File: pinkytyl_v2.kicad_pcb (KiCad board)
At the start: 2 copper layers, 132 x 105.9 mm, 62 parts, among them J1 50-00174, J2 Conn_01x02, J3 USB_B_Mini, J5 Conn_02x05_Odd_Even, K0 KEYSW, K10 KEYSW, K11 KEYSW, K12 KEYSW, K13 KEYSW, K14 KEYSW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

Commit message: Adds name to silkscreen
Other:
- board text added: "ISP"
- board text added: "Pinkytyl V2 By Philip K. Gisslow 09/27/21"
- board text added: "Reset"
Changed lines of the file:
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@@
   (general
     (thickness 1.6)
-    (drawings 33)
+    (drawings 36)
     (tracks 605)
     (zones 0)
@@
     (descr "Through hole straight pin header, 1x02, 1.27mm pitch, single row")
     (tags "Through hole pin header THT 1x02 1.27mm single row")
-    (fp_text reference J2 (at -2.51 0.31 90) (layer F.SilkS)
+    (fp_text reference J2 (at -0.03 -2.34 90) (layer F.SilkS)
       (effects (font (size 1 1) (thickness 0.15)))
     )
@@
     (tags capacitor)
     (attr smd)
-    (fp_text reference C6 (at 2.69 1.52) (layer F.SilkS)
+    (fp_text reference C6 (at -4.79 0.41) (layer F.SilkS)
       (effects (font (size 1 1) (thickness 0.15)))
     )
@@
     )
   )
+  (gr_text ISP (at 186.4 116.18) (layer F.SilkS)
+    (effects (font (size 1 1) (thickness 0.15)))
+  )
+  (gr_text Reset (at 185.94 111.68) (layer F.SilkS)
+    (effects (font (size 1 1) (thickness 0.15)))
+  )
+  (gr_text "Pinkytyl V2 By\nPhilip K. Gisslow\n09/27/21" (at 174.81 117.05) (layer F.SilkS)
+    (effects (font (size 1 1) (thickness 0.15)))
+  )
   (gr_line (start 130.716898 92.180109) (end 125.716898 100.724303) (layer Edge.Cuts) (width 0.2))

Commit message: Inc
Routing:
- net VCC: track 238.5 -> 246.6 mm
- net r0: track 160.7 -> 157.3 mm
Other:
- board text added: "JLCJLCJLCJLC"
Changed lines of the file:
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@@
   (general
     (thickness 1.6)
-    (drawings 36)
-    (tracks 605)
+    (drawings 37)
+    (tracks 602)
     (zones 0)
     (modules 62)
@@
     )
   )
+  (gr_text JLCJLCJLCJLC (at 163.01 107.25) (layer F.SilkS)
+    (effects (font (size 0.9 0.9) (thickness 0.15)))
+  )
   (gr_text ISP (at 186.4 116.18) (layer F.SilkS)
     (effects (font (size 1 1) (thickness 0.15)))
@@
   (segment (start 155.17 106.02) (end 155.14 106.05) (width 0.25) (layer F.Cu) (net 1))
   (segment (start 155.17 104.87) (end 155.17 106.02) (width 0.25) (layer F.Cu) (net 1))
-  (via (at 156.67 113.63) (size 0.8) (drill 0.4) (layers F.Cu B.Cu) (net 1))
-  (segment (start 155.14 112.1) (end 156.67 113.63) (width 0.25) (layer B.Cu) (net 1))
-  (segment (start 155.14 106.05) (end 155.14 112.1) (width 0.25) (layer B.Cu) (net 1))
-  (segment (start 158.78 113.63) (end 158.92 113.77) (width 0.25) (layer F.Cu) (net 1))
-  (segment (start 156.67 113.63) (end 158.78 113.63) (width 0.25) (layer F.Cu) (net 1))
-  (segment (start 166.655001 112.694999) (end 166.92 112.959998) (width 0.25) (layer F.Cu) (net 1))
-  (segment (start 162.239132 111.305542) (end 163.628589 112.694999) (width 0.25) (layer F.Cu) (net 1))
-  (segment (start 163.628589 112.694999) (end 166.655001 112.694999) (width 0.25) (layer F.Cu) (net 1))
-  (segment (start 159.819186 111.305542) (end 162.239132 111.305542) (width 0.25) (layer F.Cu) (net 1))
-  (segment (start 158.429729 112.694999) (end 159.819186 111.305542) (width 0.25) (layer F.Cu) (net 1))
-  (segment (start 166.92 112.959998) (end 166.92 113.77) (width 0.25) (layer F.Cu) (net 1))
-  (segment (start 157.605001 112.694999) (end 158.429729 112.694999) (width 0.25) (layer F.Cu) (net 1))
-  (segment (start 156.67 113.63) (end 157.605001 112.694999) (width 0.25) (layer F.Cu) (net 1))
   (segment (start 169.93 101.24) (end 169.02 100.33) (width 0.25) (layer F.Cu) (net 1))
   (segment (start 170.82 101.24) (end 169.93 101.24) (width 0.25) (layer F.Cu) (net 1))
   (segment (start 169.02 102.83) (end 168.404999 103.445001) (width 0.25) (layer F.Cu) (net 1))
   (segment (start 169.02 100.33) (end 169.02 102.83) (width 0.25) (layer F.Cu) (net 1))
+  (segment (start 163.628589 112.694999) (end 162.239132 111.305542) (width 0.25) (layer F.Cu) (net 1))
+  (segment (start 166.92 112.77) (end 166.844999 112.694999) (width 0.25) (layer F.Cu) (net 1))
+  (via (at 161.46 117.05) (size 0.8) (drill 0.4) (layers F.Cu B.Cu) (net 1))
+  (segment (start 158.92 113.77) (end 158.920001 115.140001) (width 0.25) (layer F.Cu) (net 1))
+  (segment (start 159.788773 111.305542) (end 158.920001 112.174314) (width 0.25) (layer F.Cu) (net 1))
+  (segment (start 160.83 117.05) (end 161.46 117.05) (width 0.25) (layer F.Cu) (net 1))
+  (segment (start 158.920001 115.140001) (end 160.83 117.05) (width 0.25) (layer F.Cu) (net 1))
+  (segment (start 166.844999 112.694999) (end 163.628589 112.694999) (width 0.25) (layer F.Cu) (net 1))
+  (segment (start 162.239132 111.305542) (end 159.788773 111.305542) (width 0.25) (layer F.Cu) (net 1))
+  (segment (start 155.14 110.73) (end 161.46 117.05) (width 0.25) (layer B.Cu) (net 1))
+  (segment (start 166.92 113.77) (end 166.92 112.77) (width 0.25) (layer F.Cu) (net 1))
+  (segment (start 155.14 106.05) (end 155.14 110.73) (width 0.25) (layer B.Cu) (net 1))
+  (segment (start 158.920001 112.174314) (end 158.920001 115.140001) (width 0.25) (layer F.Cu) (net 1))
   (segment (start 116.54 44.4725) (end 115.34 44.4725) (width 0.25) (layer F.Cu) (net 2))
   (segment (start 157.06 103.91) (end 157.22 104.07) (width 0.25) (layer F.Cu) (net 2))
@@
   (segment (start 163.81609 96.82391) (end 163.85 96.79) (width 0.25) (layer F.Cu) (net 2))
   (segment (start 155.94 96.82391) (end 163.81609 96.82391) (width 0.25) (layer F.Cu) (net 2))
-  (segment (start 159.72 114.77) (end 159.72 113.77) (width 0.25) (layer F.Cu) (net 2))
-  (segment (start 161.18501 116.23501) (end 159.72 114.77) (width 0.25) (layer F.Cu) (net 2))
-  (segment (start 166.02499 116.23501) (end 161.18501 116.23501) (width 0.25) (layer F.Cu) (net 2))
-  (segment (start 166.35 115.91) (end 166.02499 116.23501) (width 0.25) (layer F.Cu) (net 2))
-  (segment (start 166.35 115.6) (end 166.35 115.91) (width 0.25) (layer F.Cu) (net 2))
   (segment (start 173.77 107.27) (end 172.04 107.27) (width 0.25) (layer F.Cu) (net 2))
   (segment (start 174.23 107.73) (end 173.77 107.27) (width 0.25) (layer F.Cu) (net 2))
@@
   (segment (start 162.2 97.994315) (end 163.404315 96.79) (width 0.25) (layer F.Cu) (net 2))
   (segment (start 162.2 98.56) (end 162.2 97.994315) (width 0.25) (layer F.Cu) (net 2))
+  (segment (start 166.02499 116.23501) (end 161.378012 116.23501) (width 0.25) (layer F.Cu) (net 2))
+  (segment (start 166.35 115.91) (end 166.02499 116.23501) (width 0.25) (layer F.Cu) (net 2))
+  (segment (start 166.35 115.6) (end 166.35 115.91) (width 0.25) (layer F.Cu) (net 2))
+  (segment (start 159.72 114.576998) (end 159.72 113.77) (width 0.25) (layer F.Cu) (net 2))
+  (segment (start 161.378012 116.23501) (end 159.72 114.576998) (width 0.25) (layer F.Cu) (net 2))
   (segment (start 163.85 99.66) (end 163.56 99.95) (width 0.25) (layer F.Cu) (net 3))
   (segment (start 163.85 98.49) (end 163.85 99.66) (width 0.25) (layer F.Cu) (net 3))
@@
   (segment (start 85.657358 123.3) (end 79.04 116.682642) (width 0.25) (layer F.Cu) (net 22))
   (segment (start 89.05 123.3) (end 85.657358 123.3) (width 0.25) (layer F.Cu) (net 22))
-  (segment (start 99.84 114.99) (end 99.84 108.82) (width 0.25) (layer F.Cu) (net 22))
-  (segment (start 142.2 88.86) (end 151.24 97.9) (width 0.25) (layer F.Cu) (net 22))
+  (segment (start 153.73 100.39) (end 153.73 107.238427) (width 0.25) (layer F.Cu) (net 22))
+  (segment (start 142.2 88.86) (end 153.73 100.39) (width 0.25) (layer F.Cu) (net 22))
   (segment (start 127.82 88.86) (end 142.2 88.86) (width 0.25) (layer F.Cu) (net 22))
+  (segment (start 121.47 95.21) (end 127.82 88.86) (width 0.25) (layer F.Cu) (net 22))
   (segment (start 113.45 95.21) (end 121.47 95.21) (width 0.25) (layer F.Cu) (net 22))
   (segment (start 99.84 108.82) (end 113.45 95.21) (width 0.25) (layer F.Cu) (net 22))
-  (segment (start 89.05 123.3) (end 92.472642 123.3) (width 0.25) (layer F.Cu) (net 22))
-  (segment (start 92.472642 123.3) (end 96.238001 119.534641) (width 0.25) (layer F.Cu) (net 22))
-  (segment (start 121.47 95.21) (end 127.82 88.86) (width 0.25) (layer F.Cu) (net 22))
+  (segment (start 99.84 114.99) (end 99.84 108.82) (width 0.25) (layer F.Cu) (net 22))
   (segment (start 96.238001 118.591999) (end 99.84 114.99) (width 0.25) (layer F.Cu) (net 22))
   (segment (start 96.238001 119.534641) (end 96.238001 118.591999) (width 0.25) (layer F.Cu) (net 22))
-  (segment (start 151.24 97.9) (end 151.24 107.103269) (width 0.25) (layer F.Cu) (net 22))
-  (segment (start 151.363146 107.27) (end 151.331573 107.238427) (width 0.25) (layer F.Cu) (net 22))
-  (segment (start 157.22 107.27) (end 151.363146 107.27) (width 0.25) (layer F.Cu) (net 22))
-  (segment (start 151.24 107.103269) (end 151.331573 107.238427) (width 0.25) (layer F.Cu) (net 22))
-  (segment (start 162.320272 120.093274) (end 162.666878 120.093274) (width 0.25) (layer F.Cu) (net 22))
-  (segment (start 157.319985 115.092987) (end 162.320272 120.093274) (width 0.25) (layer F.Cu) (net 22))
-  (segment (start 157.022987 115.092987) (end 157.319985 115.092987) (width 0.25) (layer F.Cu) (net 22))
-  (segment (start 155.876163 113.946163) (end 157.022987 115.092987) (width 0.25) (layer F.Cu) (net 22))
-  (segment (start 162.666878 120.093274) (end 163.303274 120.093274) (width 0.25) (layer F.Cu) (net 22))
-  (segment (start 151.331573 107.238427) (end 155.876163 113.946163) (width 0.25) (layer F.Cu) (net 22))
+  (segment (start 92.472642 123.3) (end 96.238001 119.534641) (width 0.25) (layer F.Cu) (net 22))
+  (segment (start 89.05 123.3) (end 92.472642 123.3) (width 0.25) (layer F.Cu) (net 22))
+  (segment (start 157.188427 107.238427) (end 157.22 107.27) (width 0.25) (layer F.Cu) (net 22))
+  (segment (start 155.758427 112.614837) (end 163.236864 120.093274) (width 0.25) (layer F.Cu) (net 22))
+  (segment (start 163.236864 120.093274) (end 163.303274 120.093274) (width 0.25) (layer F.Cu) (net 22))
+  (segment (start 155.758427 107.238427) (end 155.758427 112.614837) (width 0.25) (layer F.Cu) (net 22))
+  (segment (start 153.73 107.238427) (end 155.758427 107.238427) (width 0.25) (layer F.Cu) (net 22))
+  (segment (start 155.758427 107.238427) (end 157.188427 107.238427) (width 0.25) (layer F.Cu) (net 22))
   (segment (start 77.02 117.57) (end 77.02 116.3) (width 0.25) (layer F.Cu) (net 23))
   (segment (start 75.75 118.84) (end 77.02 117.57) (width 0.25) (layer F.Cu) (net 23))

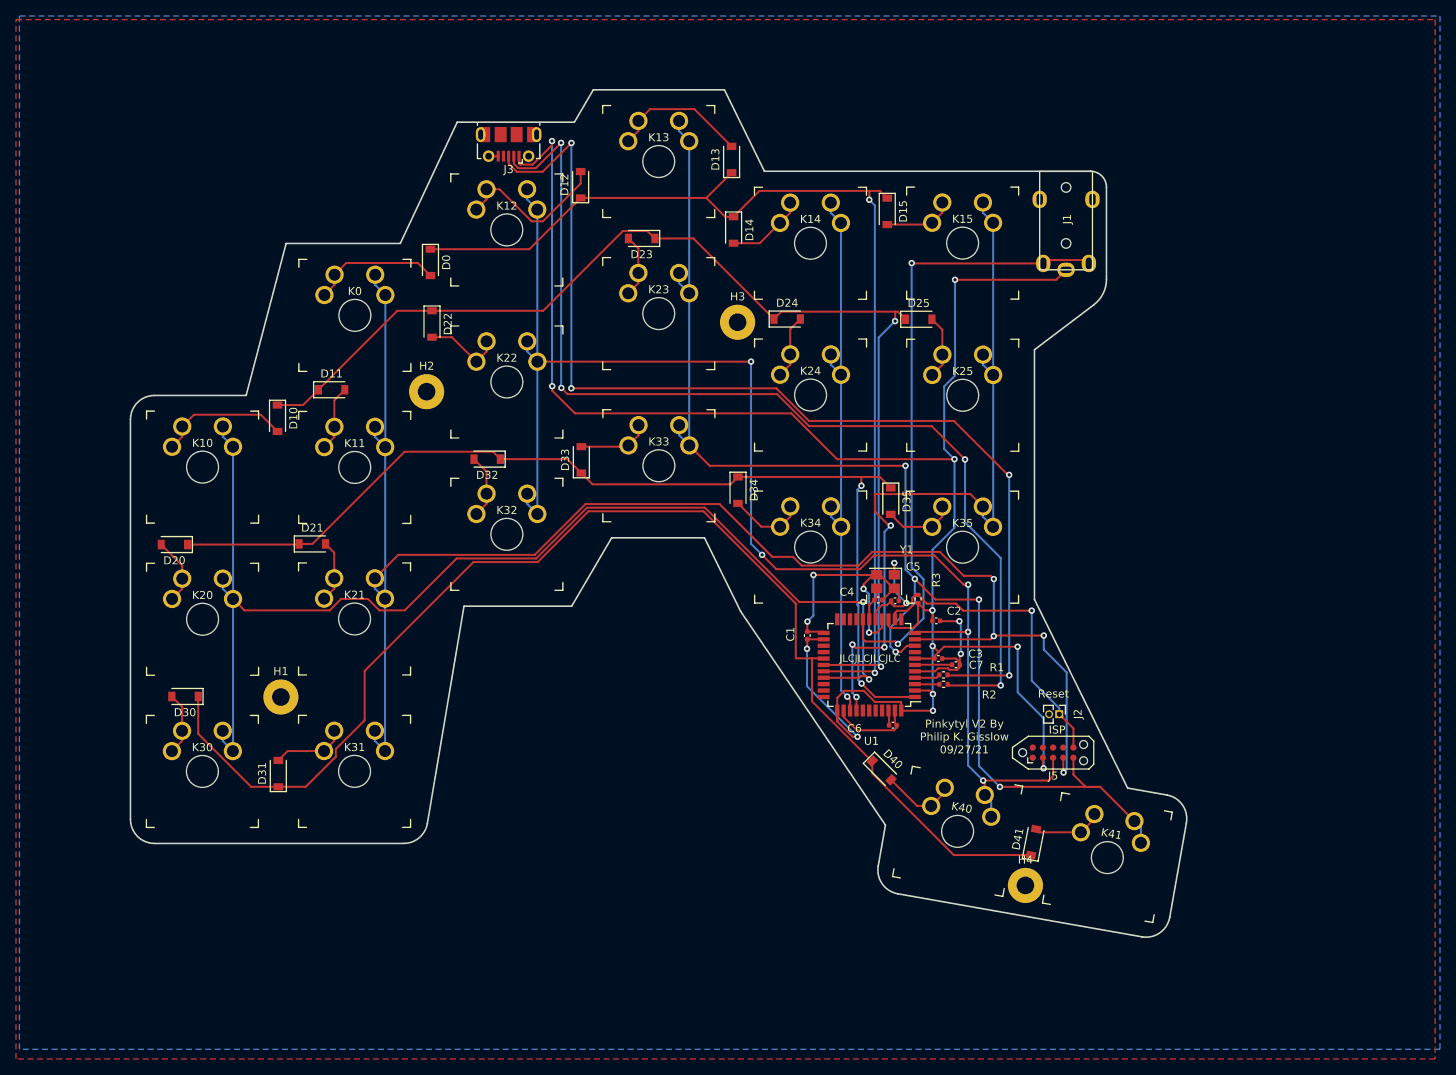
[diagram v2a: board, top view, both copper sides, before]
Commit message: Adds mounting holes
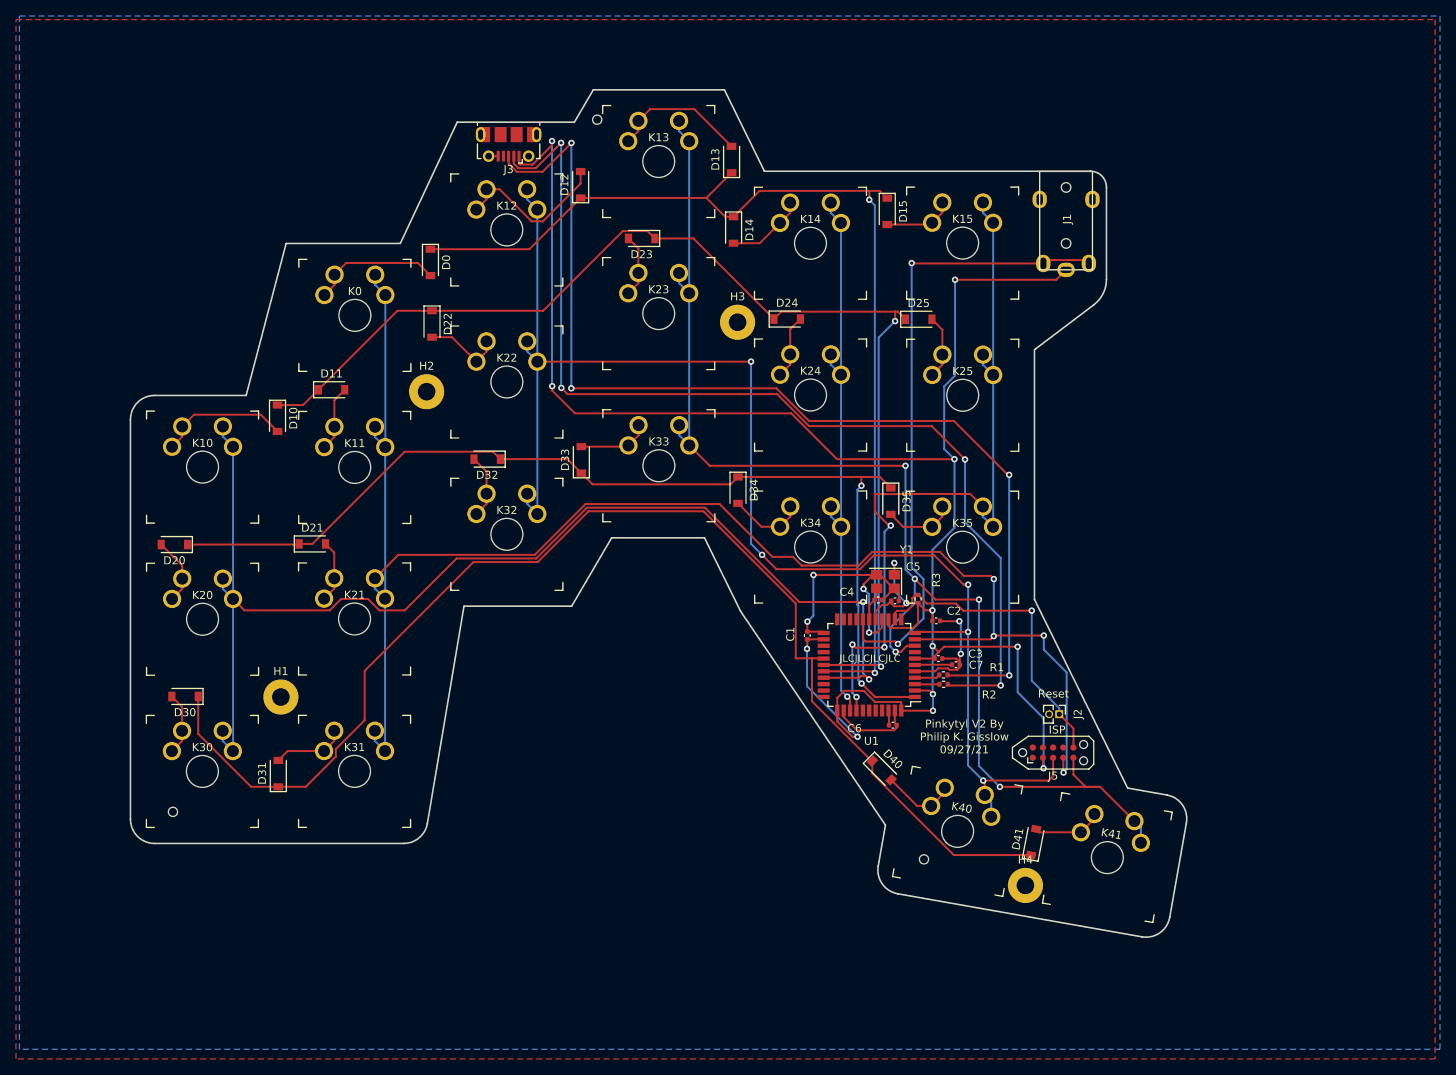
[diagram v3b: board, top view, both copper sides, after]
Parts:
- added REF**: MountingHole_1.152mm, Logos:JLCPCB_MountingHole_1.152mm, F.Cu at (128.9, 39.9)
- added REF**: MountingHole_1.152mm, Logos:JLCPCB_MountingHole_1.152mm, F.Cu at (169.8, 132.4)
- added REF**: MountingHole_1.152mm, Logos:JLCPCB_MountingHole_1.152mm, F.Cu at (75.9, 126.4)

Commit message: Initial commit for chocs
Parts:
- added D1: D, Diode_SMD:D_SOD-123, F.Cu at (125.5, 42.3)
- K0, K10, K11, K12, K13, K14, K15, K20, K21, K22, K23, K24, K25, K30, K31, K32, K33, K34, K35, K40, K41: footprint keyswitches:SW_MX_reversible_minimal -> keyswitches:SW_PG1350_reversible
- moved REF** 7.60 mm to (136.5, 40.1)
- moved C3 7.55 mm to (170.7, 114.8), turned to 270 degrees
- moved REF** 5.64 mm to (175.3, 133.6)
- moved R3 2.26 mm to (171.0, 100.9), turned to 0 degrees
- moved REF** 1.03 mm to (76.9, 126.5)
- moved C7 0.45 mm to (173.7, 107.6), turned to 90 degrees
- moved C1 0.44 mm to (154.7, 104.4)
- turned C4 to 180 degrees
- turned D31 to 270 degrees
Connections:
- J3 pad 1: VCC -> UVCC
- U1 pad 33: Net-(U1-Pad33) -> GND
- U1 pad 7: VCC -> UVCC
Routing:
- net UVCC: track 0.00 -> 116.1 mm, vias 0 -> 4
- net VCC: track 246.6 -> 208.6 mm, vias 12 -> 7
- net MISO: track 175.6 -> 211.8 mm
- net MOSI: track 199.6 -> 234.8 mm
- net r0: track 157.3 -> 190.0 mm, vias 0 -> 6
- net c0: track 153.9 -> 176.5 mm, vias 2 -> 4
- net GND: track 64.8 -> 42.9 mm, vias 6 -> 2
- net c3: track 164.6 -> 185.9 mm
- net c4: track 70.6 -> 89.9 mm
- net Net-(D24-Pad2): track 8.01 -> 20.1 mm, vias 0 -> 1
- net Net-(D34-Pad2): track 9.55 -> 19.1 mm, vias 0 -> 1
- net Net-(D11-Pad2): track 8.23 -> 17.4 mm, vias 0 -> 1
- net Net-(D22-Pad2): track 9.88 -> 18.9 mm, vias 0 -> 1
- net Net-(D32-Pad2): track 8.04 -> 17.0 mm, vias 0 -> 1
- net Net-(D30-Pad2): track 7.89 -> 16.9 mm, vias 0 -> 1
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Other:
- board text added: "Pinkytyl V2.1 By Philip K. Gisslow 09/27/21"
- board text removed: "JLCJLCJLCJLC"
- board text removed: "Pinkytyl V2 By Philip K. Gisslow 09/27/21"
